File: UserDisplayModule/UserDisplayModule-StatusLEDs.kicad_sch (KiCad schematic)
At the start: 23 parts, among them U1 74HC595

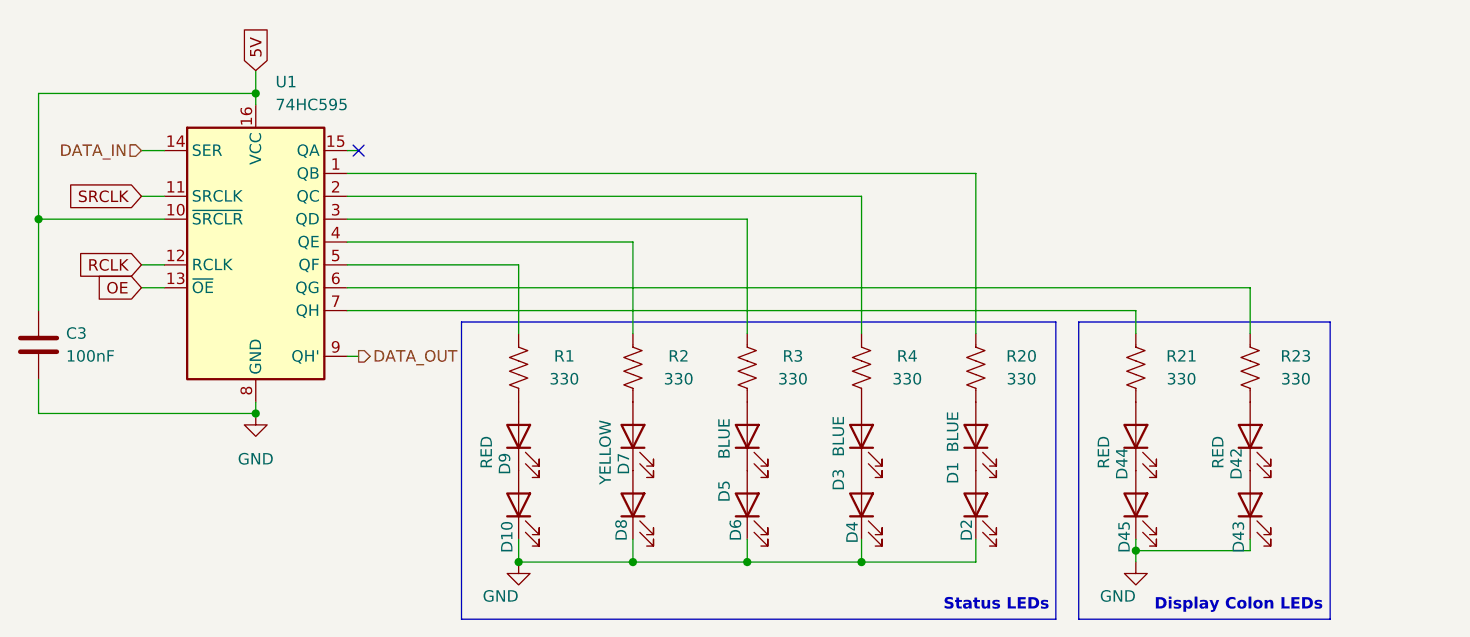
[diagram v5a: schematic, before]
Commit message: Edited BOM for R/C parts
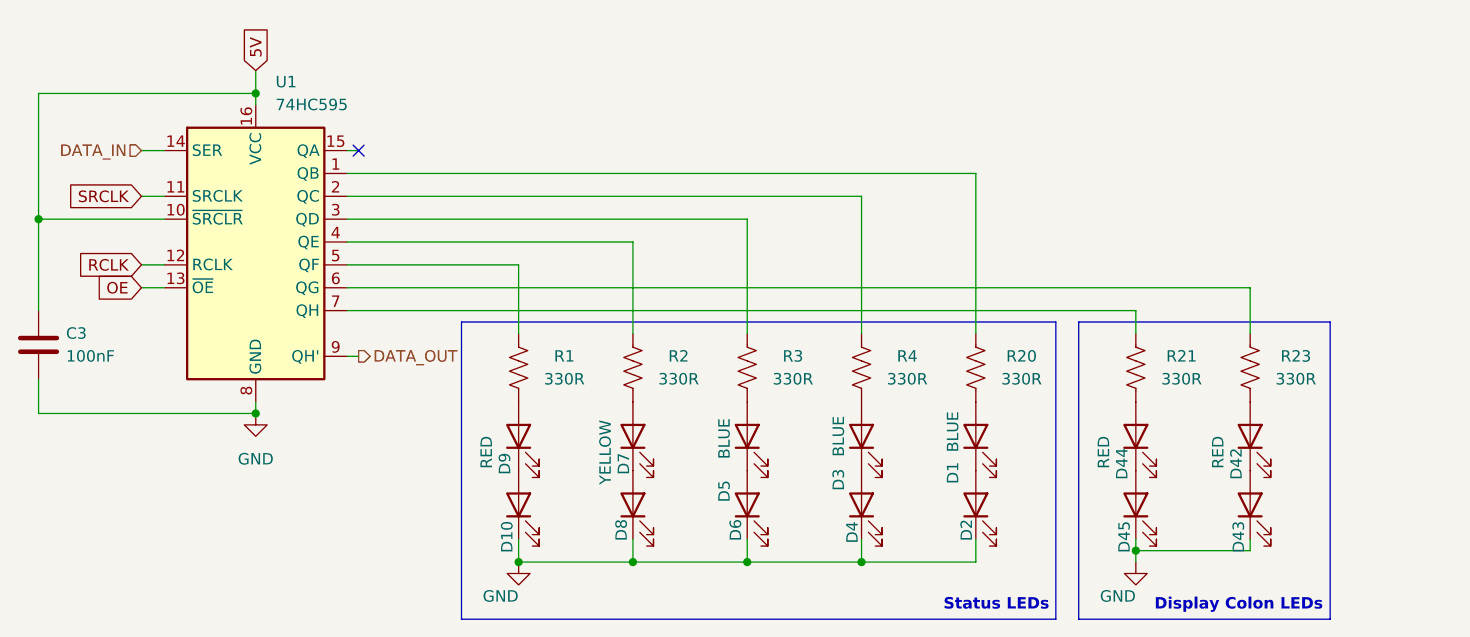
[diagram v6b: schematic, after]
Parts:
- C3: Digikey PN (none) -> 1276-1003-1-ND
- R1, R2, R20, R21, R23, R3, R4: value 330 -> 330R; Digikey PN (none) -> RMCF0805FT330RCT-ND
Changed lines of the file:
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@@
 			)
 		)
-		(property "Value" "330"
+		(property "Value" "330R"
 			(at 205.74 99.06 0)
 			(effects
@@
 			)
 		)
-		(property "Digikey PN" ""
+		(property "Digikey PN" "RMCF0805FT330RCT-ND"
 			(at 200.66 97.79 0)
 			(effects
@@
 			)
 		)
-		(property "Value" "330"
+		(property "Value" "330R"
 			(at 124.46 99.06 0)
 			(effects
@@
 			)
 		)
-		(property "Digikey PN" ""
+		(property "Digikey PN" "RMCF0805FT330RCT-ND"
 			(at 119.38 97.79 0)
 			(effects
@@
 			)
 		)
-		(property "Value" "330"
+		(property "Value" "330R"
 			(at 149.86 99.06 0)
 			(effects
@@
 			)
 		)
-		(property "Digikey PN" ""
+		(property "Digikey PN" "RMCF0805FT330RCT-ND"
 			(at 144.78 97.79 0)
 			(effects
@@
 			)
 		)
-		(property "Value" "330"
+		(property "Value" "330R"
 			(at 193.04 99.06 0)
 			(effects
@@
 			)
 		)
-		(property "Digikey PN" ""
+		(property "Digikey PN" "RMCF0805FT330RCT-ND"
 			(at 187.96 97.79 0)
 			(effects
@@
 			)
 		)
-		(property "Value" "330"
+		(property "Value" "330R"
 			(at 175.26 99.06 0)
 			(effects
@@
 			)
 		)
-		(property "Digikey PN" ""
+		(property "Digikey PN" "RMCF0805FT330RCT-ND"
 			(at 170.18 97.79 0)
 			(effects
@@
 			)
 		)
-		(property "Value" "330"
+		(property "Value" "330R"
 			(at 137.16 99.06 0)
 			(effects
@@
 			)
 		)
-		(property "Digikey PN" ""
+		(property "Digikey PN" "RMCF0805FT330RCT-ND"
 			(at 132.08 97.79 0)
 			(effects
@@
 			)
 		)
-		(property "Value" "330"
+		(property "Value" "330R"
 			(at 162.56 99.06 0)
 			(effects
@@
 			)
 		)
-		(property "Digikey PN" ""
+		(property "Digikey PN" "RMCF0805FT330RCT-ND"
 			(at 157.48 97.79 0)
 			(effects
@@
 			)
 		)
-		(property "Digikey PN" ""
+		(property "Digikey PN" "1276-1003-1-ND"
 			(at 66.04 95.25 0)
 			(effects
